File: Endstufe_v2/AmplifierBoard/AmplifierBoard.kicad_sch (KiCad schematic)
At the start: 19 parts, among them J10 Conn_02x06_Top_Bottom, J11 B6B-XH-2(LF)(SN), J12 B6B-XH-2(LF)(SN), J13 Conn_01x02_Pin, J14 Conn_01x02_Pin, J15 Conn_01x02_Pin, J16 Conn_01x04, J9 ST-0322D00-071-1A2H, U3 NVTFWS014P04M8LTAG, U4 1SMA5927A

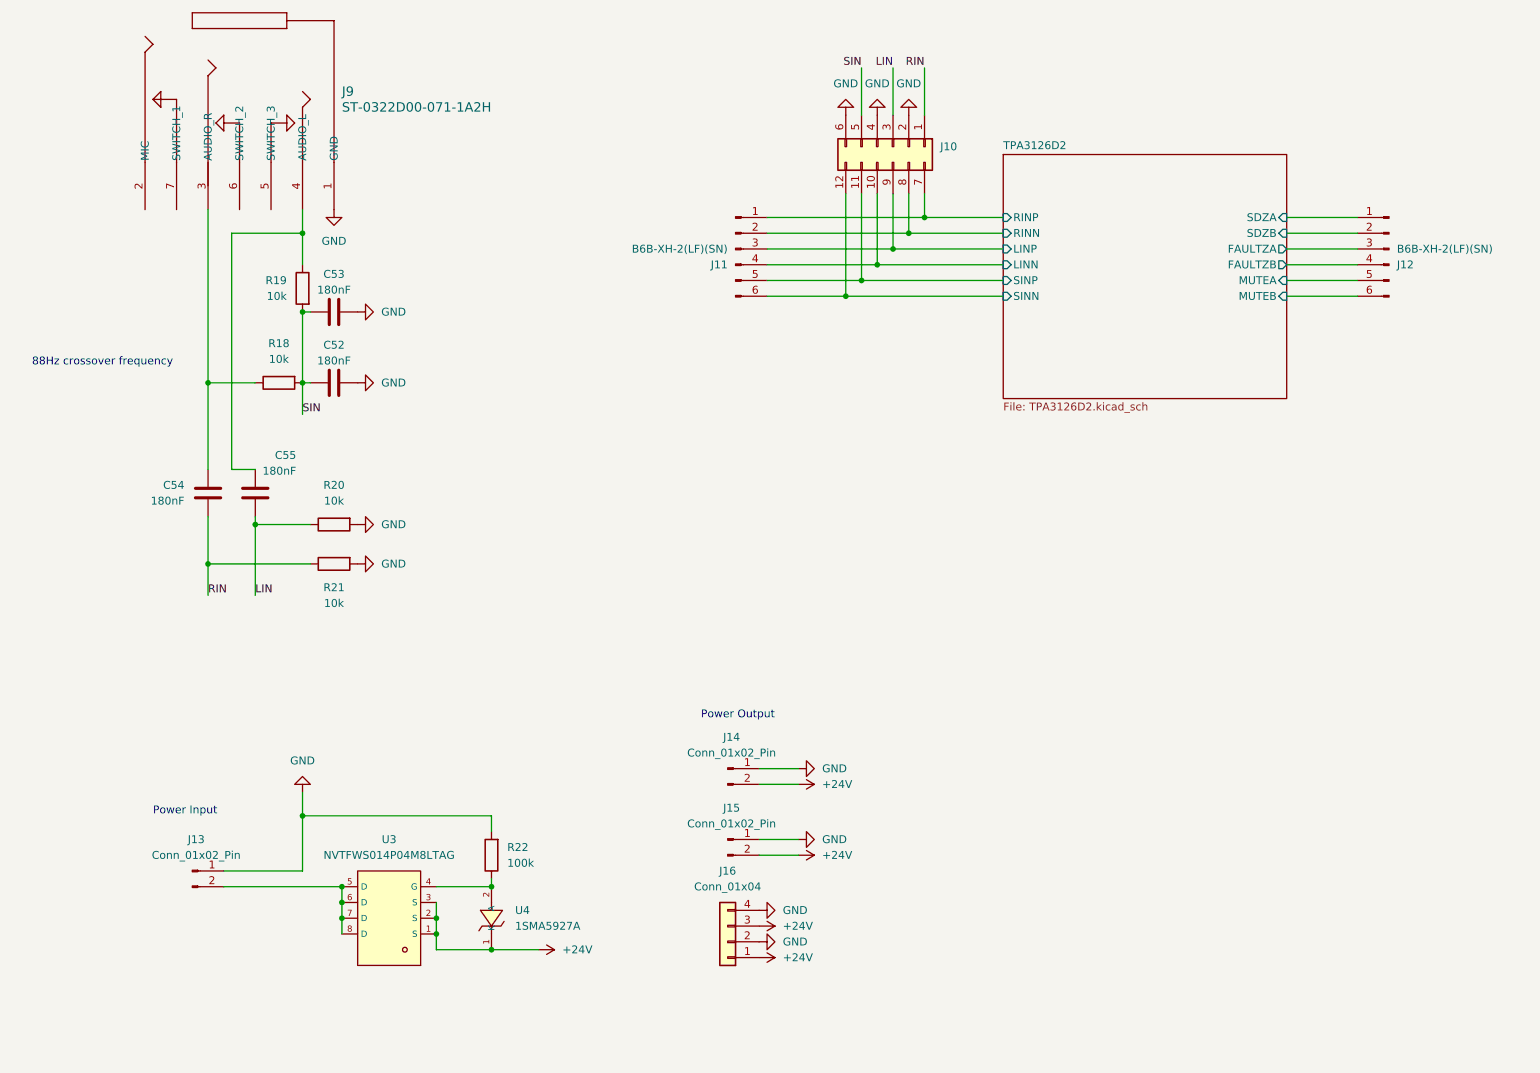
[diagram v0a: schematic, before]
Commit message: Layout amplifier board
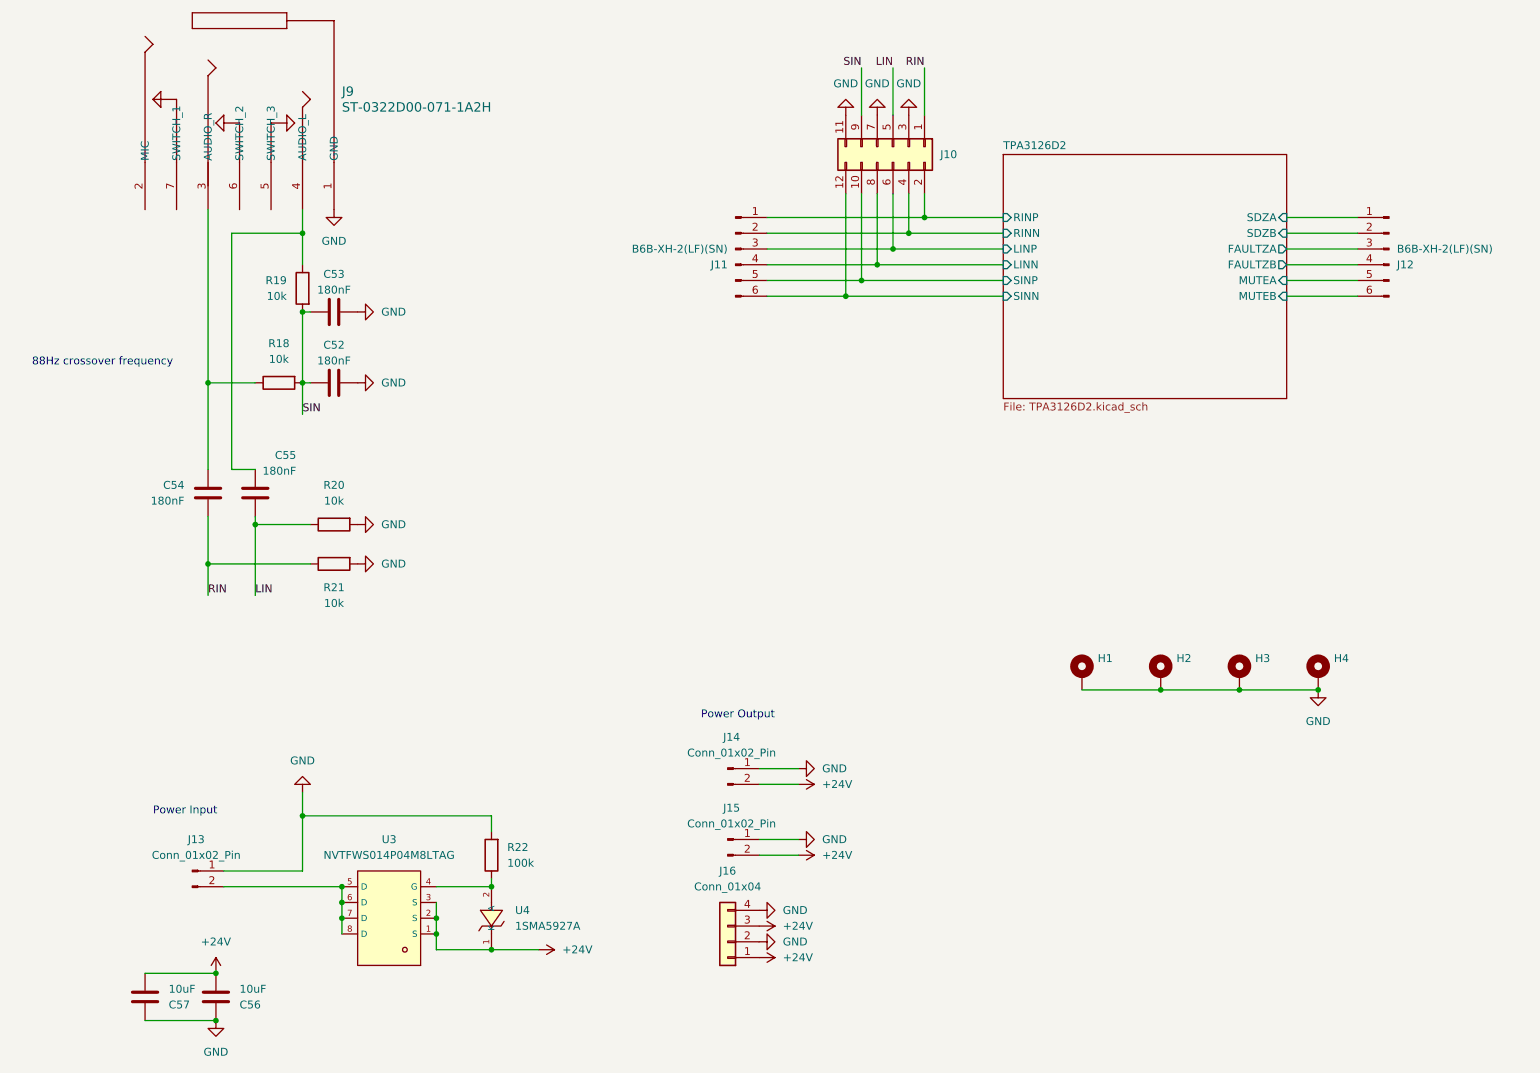
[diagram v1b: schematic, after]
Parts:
- added C56, C57: 10uF, Endstufe:C_1206_3216Metric, symbol Endstufe:C
- added H1, H2, H3, H4: MountingHole_Pad, MountingHole:MountingHole_2.2mm_M2_ISO7380_Pad, symbol Endstufe:MountingHole_Pad
- J10: footprint (none) -> Connector_PinHeader_2.54mm:PinHeader_2x06_P2.54mm_Vertical; symbol Connector_Generic:Conn_02x06_Top_Bottom -> Connector_Generic:Conn_02x06_Odd_Even
- J16: footprint (none) -> Connector_PinHeader_2.54mm:PinHeader_1x04_P2.54mm_Vertical
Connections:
- net +24V: now also C56.2, C57.2
- net GND: now also J10.11 (Pin_11), J10.3 (Pin_3), J10.7 (Pin_7), C56.1, C57.1, H1.1, H2.1, H3.1, H4.1; no longer J10.2 (Pin_2), J10.4 (Pin_4), J10.6 (Pin_6)
- net LIN: now also J10.5 (Pin_5); no longer J10.3 (Pin_3)
- net SIN: now also J10.9 (Pin_9); no longer J10.5 (Pin_5)
- net TPA3126D2/LINN: now also J10.8 (Pin_8); no longer J10.10 (Pin_10)
- net TPA3126D2/LINP: now also J10.6 (Pin_6); no longer J10.9 (Pin_9)
- net TPA3126D2/RINN: now also J10.4 (Pin_4); no longer J10.8 (Pin_8)
- net TPA3126D2/RINP: now also J10.2 (Pin_2); no longer J10.7 (Pin_7)
- net TPA3126D2/SINP: now also J10.10 (Pin_10); no longer J10.11 (Pin_11)

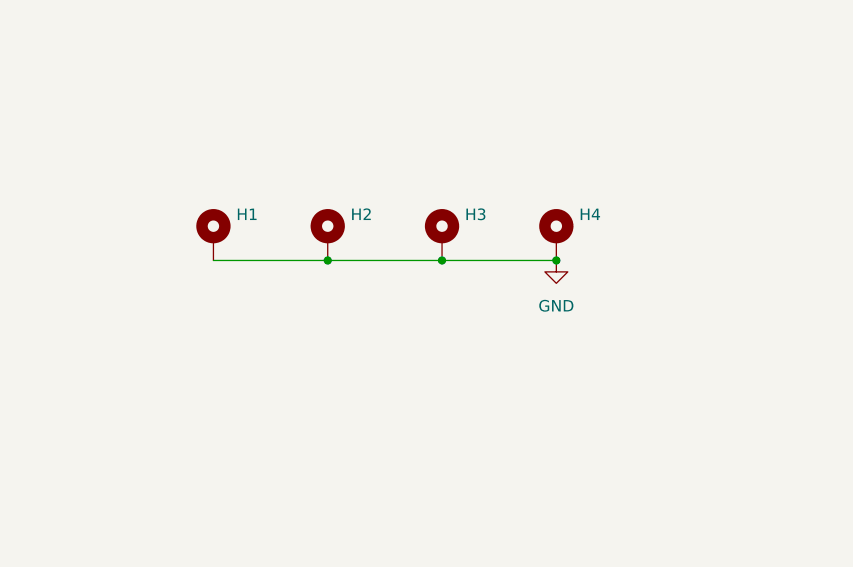
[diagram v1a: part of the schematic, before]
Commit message: Make mounting holes and continue layouting
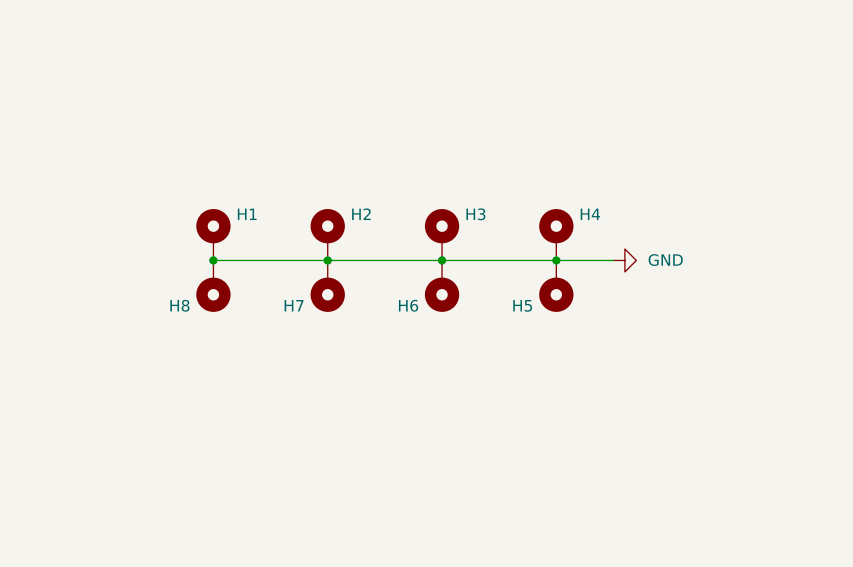
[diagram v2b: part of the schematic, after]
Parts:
- added H5, H6, H7, H8: MountingHole_Pad, Endstufe:MountingHole_3.2mm_M3_ISO14580_Pad, symbol Endstufe:MountingHole_Pad
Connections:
- net GND: now also H5.1, H6.1, H7.1, H8.1

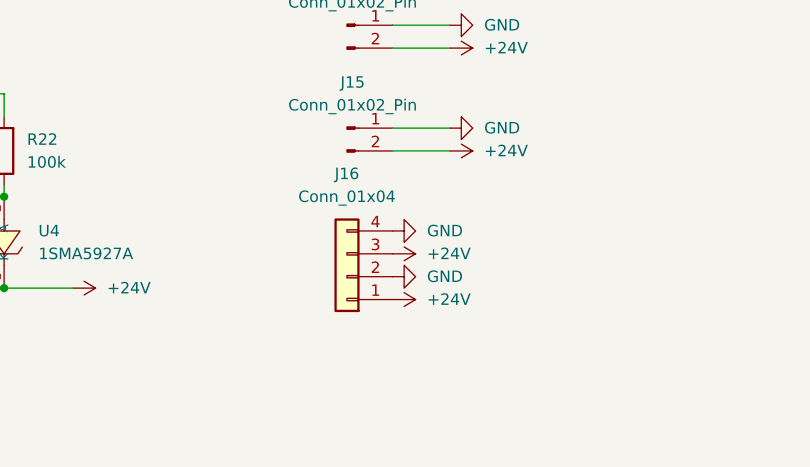
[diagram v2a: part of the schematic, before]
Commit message: Add additional power connector to amplifier board
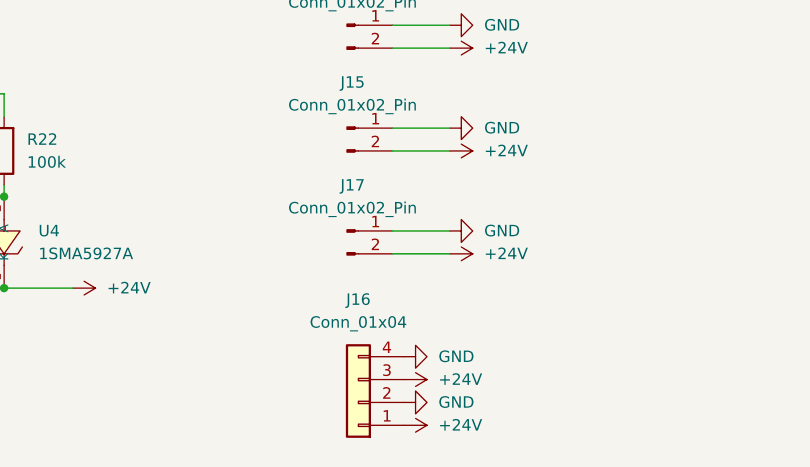
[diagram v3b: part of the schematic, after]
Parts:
- added J17: Conn_01x02_Pin, Connector_JST:JST_XH_B2B-XH-A_1x02_P2.50mm_Vertical, symbol Endstufe:Conn_01x02_Pin
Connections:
- net +24V: now also J17.2 (Pin_2)
- net GND: now also J17.1 (Pin_1)
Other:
- moved on the sheet: J16

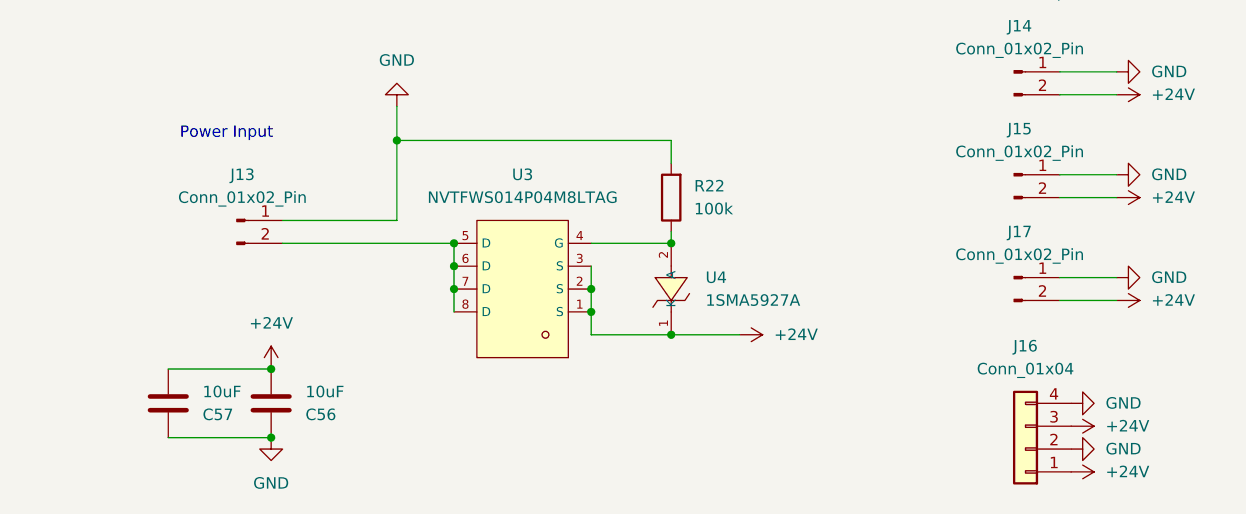
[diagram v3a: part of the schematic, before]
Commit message: Change unavailable parts to available ones, optimise silkscreen, do via stiching
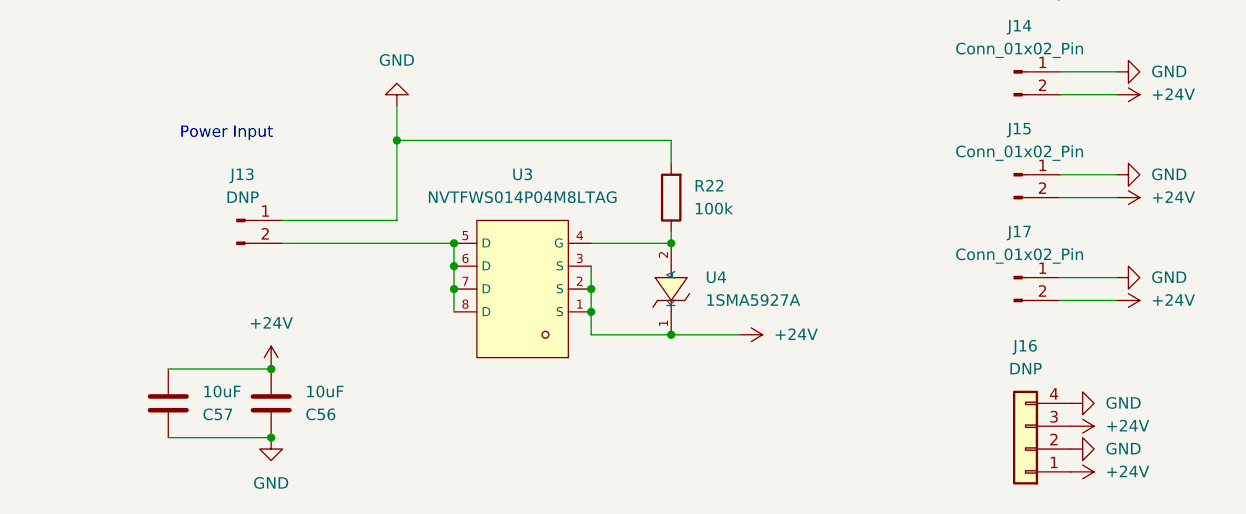
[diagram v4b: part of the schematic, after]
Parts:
- J10: value Conn_02x06_Top_Bottom -> DNP
- J11, J12: footprint Endstufe:CONN-TH_B6B-XH-2-LF-SN -> Endstufe:JST_XH_B6B-XH-A_1x06_P2.50mm_Vertical; JLCPCB Position Offset (none) -> 0,-0.5
- J13: value Conn_01x02_Pin -> DNP
- J14, J15, J17: footprint Connector_JST:JST_XH_B2B-XH-A_1x02_P2.50mm_Vertical -> Endstufe:JST_XH_B2B-XH-A_1x02_P2.50mm_Vertical; JLCPCB Position Offset (none) -> 0,-0.5; LCSC (none) -> C158012
- J16: value Conn_01x04 -> DNP
- J9: JLCPCB Position Offset (none) -> 1.5,-0.1
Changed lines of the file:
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@@
 			)
 		)
-		(property "Footprint" "Endstufe:CONN-TH_B6B-XH-2-LF-SN"
+		(property "Footprint" "Endstufe:JST_XH_B6B-XH-A_1x06_P2.50mm_Vertical"
 			(at 240.03 59.69 0)
 			(effects
@@
 		(property "LCSC" "C157986"
 			(at 240.03 59.69 0)
+			(effects
+				(font
+					(size 1.27 1.27)
+				)
+				(hide yes)
+			)
+		)
+		(property "JLCPCB Position Offset" "0,-0.5"
+			(at 480.06 119.38 0)
 			(effects
 				(font
@@
 			)
 		)
-		(property "Footprint" "Connector_JST:JST_XH_B2B-XH-A_1x02_P2.50mm_Vertical"
+		(property "Footprint" "Endstufe:JST_XH_B2B-XH-A_1x02_P2.50mm_Vertical"
 			(at 133.35 166.37 0)
 			(effects
@@
 			)
 		)
+		(property "JLCPCB Position Offset" "0,-0.5"
+			(at 0 332.74 0)
+			(effects
+				(font
+					(size 1.27 1.27)
+				)
+				(hide yes)
+			)
+		)
+		(property "LCSC" "C158012"
+			(at 0 332.74 0)
+			(effects
+				(font
+					(size 1.27 1.27)
+				)
+				(hide yes)
+			)
+		)
 		(pin "1"
 		)
@@
 			)
 		)
-		(property "Value" "Conn_01x04"
+		(property "Value" "DNP"
 			(at 134.62 176.53 0)
 			(effects
@@
 		(property "LCSC Part #" "C2829970"
 			(at 69.85 53.34 0)
+			(effects
+				(font
+					(size 1.27 1.27)
+				)
+				(hide yes)
+			)
+		)
+		(property "JLCPCB Position Offset" "1.5,-0.1"
+			(at 16.51 -16.51 0)
 			(effects
 				(font
@@
 			)
 		)
-		(property "Footprint" "Connector_JST:JST_XH_B2B-XH-A_1x02_P2.50mm_Vertical"
+		(property "Footprint" "Endstufe:JST_XH_B2B-XH-A_1x02_P2.50mm_Vertical"
 			(at 133.35 143.51 0)
 			(effects
@@
 		(property "LCSC Part #" "C158012"
 			(at 133.35 143.51 0)
+			(effects
+				(font
+					(size 1.27 1.27)
+				)
+				(hide yes)
+			)
+		)
+		(property "JLCPCB Position Offset" "0,-0.5"
+			(at 0 287.02 0)
+			(effects
+				(font
+					(size 1.27 1.27)
+				)
+				(hide yes)
+			)
+		)
+		(property "LCSC" "C158012"
+			(at 0 287.02 0)
 			(effects
 				(font
@@
 			)
 		)
-		(property "Value" "Conn_02x06_Top_Bottom"
+		(property "Value" "DNP"
 			(at 167.64 45.7199 90)
 			(effects
@@
 			)
 		)
-		(property "Footprint" "Connector_JST:JST_XH_B2B-XH-A_1x02_P2.50mm_Vertical"
+		(property "Footprint" "Endstufe:JST_XH_B2B-XH-A_1x02_P2.50mm_Vertical"
 			(at 133.35 154.94 0)
 			(effects
@@
 			)
 		)
+		(property "JLCPCB Position Offset" "0,-0.5"
+			(at 0 309.88 0)
+			(effects
+				(font
+					(size 1.27 1.27)
+				)
+				(hide yes)
+			)
+		)
+		(property "LCSC" "C158012"
+			(at 0 309.88 0)
+			(effects
+				(font
+					(size 1.27 1.27)
+				)
+				(hide yes)
+			)
+		)
 		(pin "1"
 		)
@@
 			)
 		)
-		(property "Footprint" "Endstufe:CONN-TH_B6B-XH-2-LF-SN"
+		(property "Footprint" "Endstufe:JST_XH_B6B-XH-A_1x06_P2.50mm_Vertical"
 			(at 134.62 59.69 0)
 			(effects
@@
 			)
 		)
+		(property "JLCPCB Position Offset" "0,-0.5"
+			(at 0 119.38 0)
+			(effects
+				(font
+					(size 1.27 1.27)
+				)
+				(hide yes)
+			)
+		)
 		(pin "5"
 		)
@@
 			)
 		)
-		(property "Value" "Conn_01x02_Pin"
+		(property "Value" "DNP"
 			(at 47.625 157.48 0)
 			(effects
